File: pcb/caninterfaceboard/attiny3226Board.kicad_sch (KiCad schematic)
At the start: 64 parts, among them J10 NTC2, J12 Flywheel, J13 1Wire, J2 CAN, J3 Attiny UDPI, J4 NTC3, J5 12V In, J6 FuelLevel, J7 Engine, J8 NTC1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

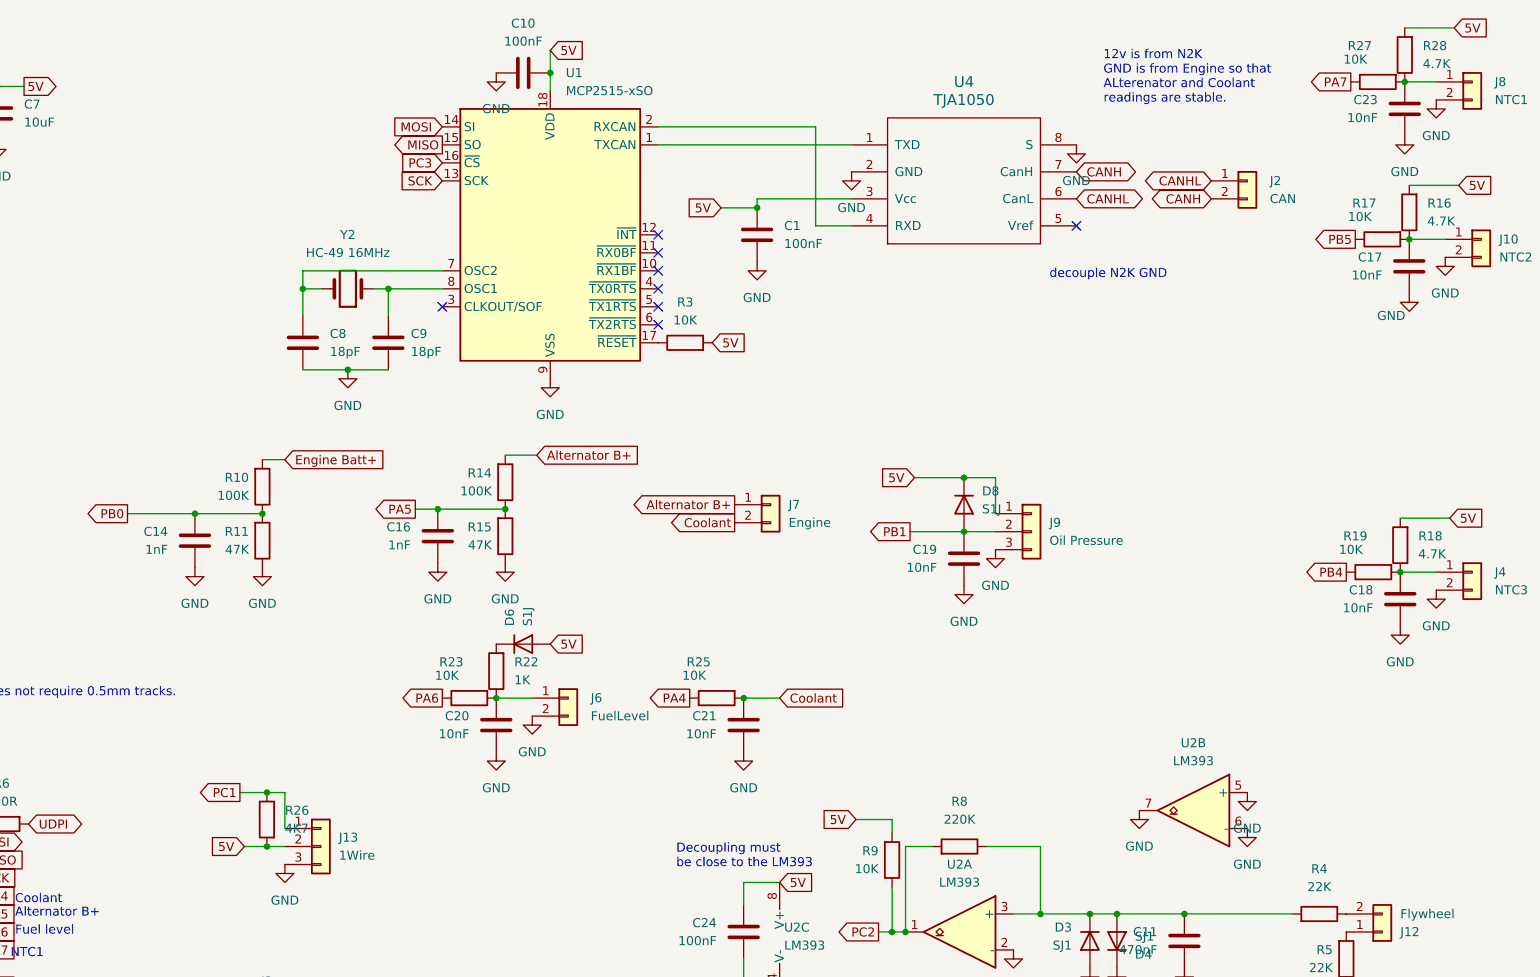
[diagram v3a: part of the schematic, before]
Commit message: Added protection for ovre voltages on measurements
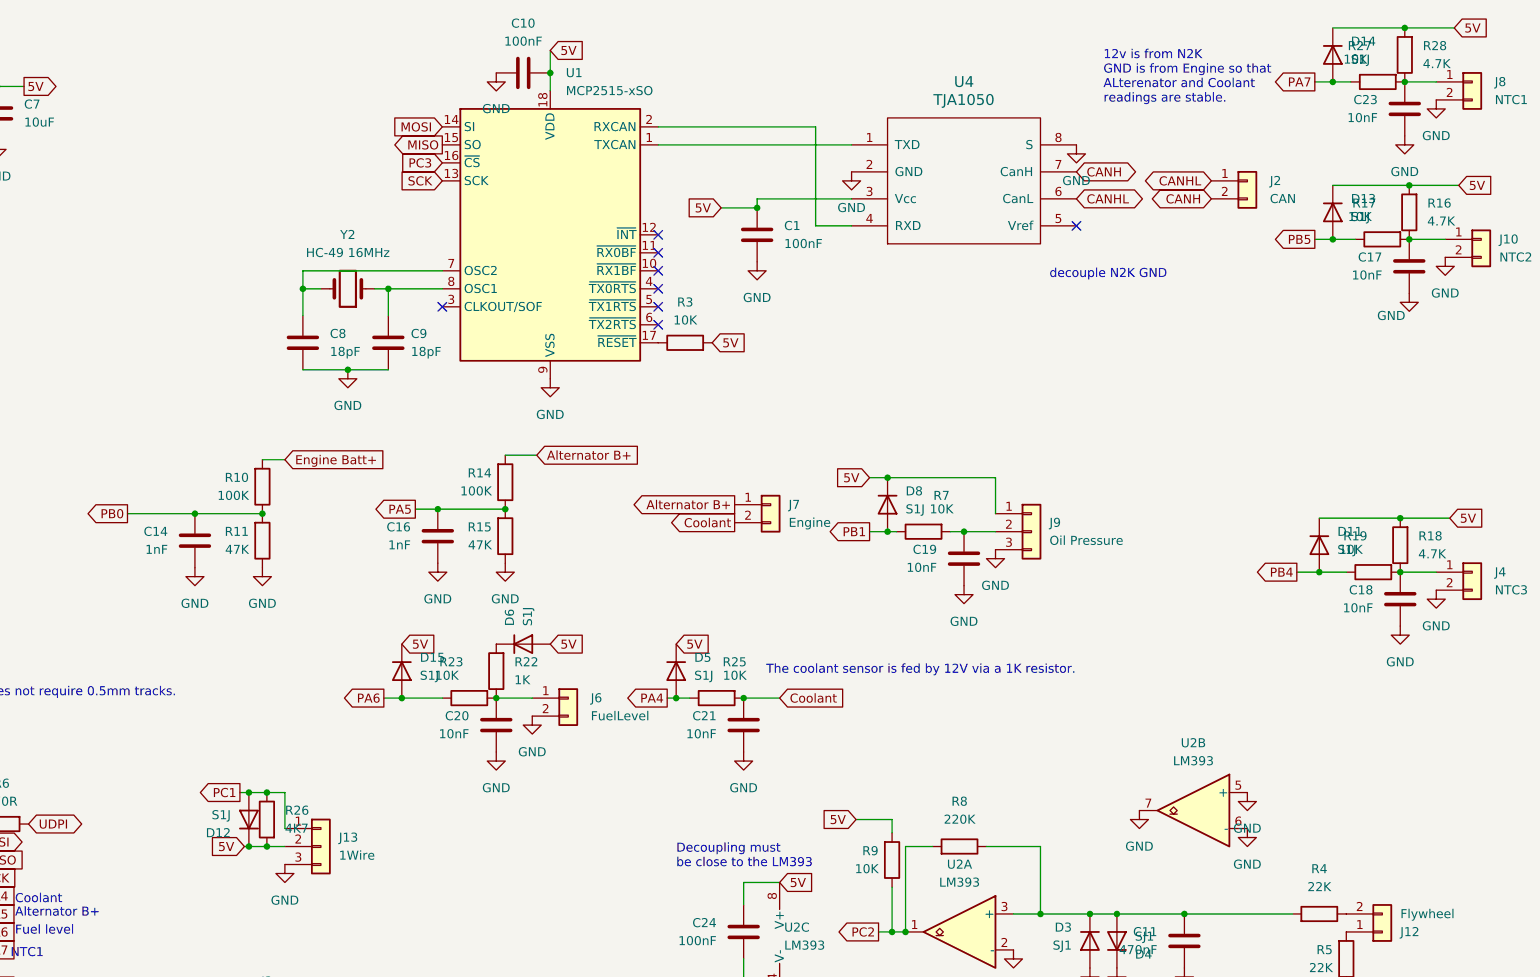
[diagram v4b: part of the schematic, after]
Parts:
- added D11, D12, D13, D14, D15, D5: S1J, Diode_SMD:D_0805_2012Metric_Pad1.15x1.40mm_HandSolder, symbol Device:D
- added R7: 10K, Resistor_SMD:R_0805_2012Metric_Pad1.20x1.40mm_HandSolder, symbol Device:R
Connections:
- net 5V: now also D11.1 (K), D12.1 (K), D13.1 (K), D14.1 (K), D15.1 (K), D5.1 (K)
- net PA4: now also D5.2 (A)
- net PA6: now also D15.2 (A)
- net PA7: now also D14.2 (A)
- net PB1: now also R7.1; no longer C19.2, J9.2 (Pin_2)
- net PB4: now also D11.2 (A)
- net PB5: now also D13.2 (A)
- net PC1: now also D12.2 (A)
- new net: C19.2, J9.2 (Pin_2), R7.2
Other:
- note added: "The coolant sensor is fed by 12V via a 1K resistor."
- moved on the sheet: D8

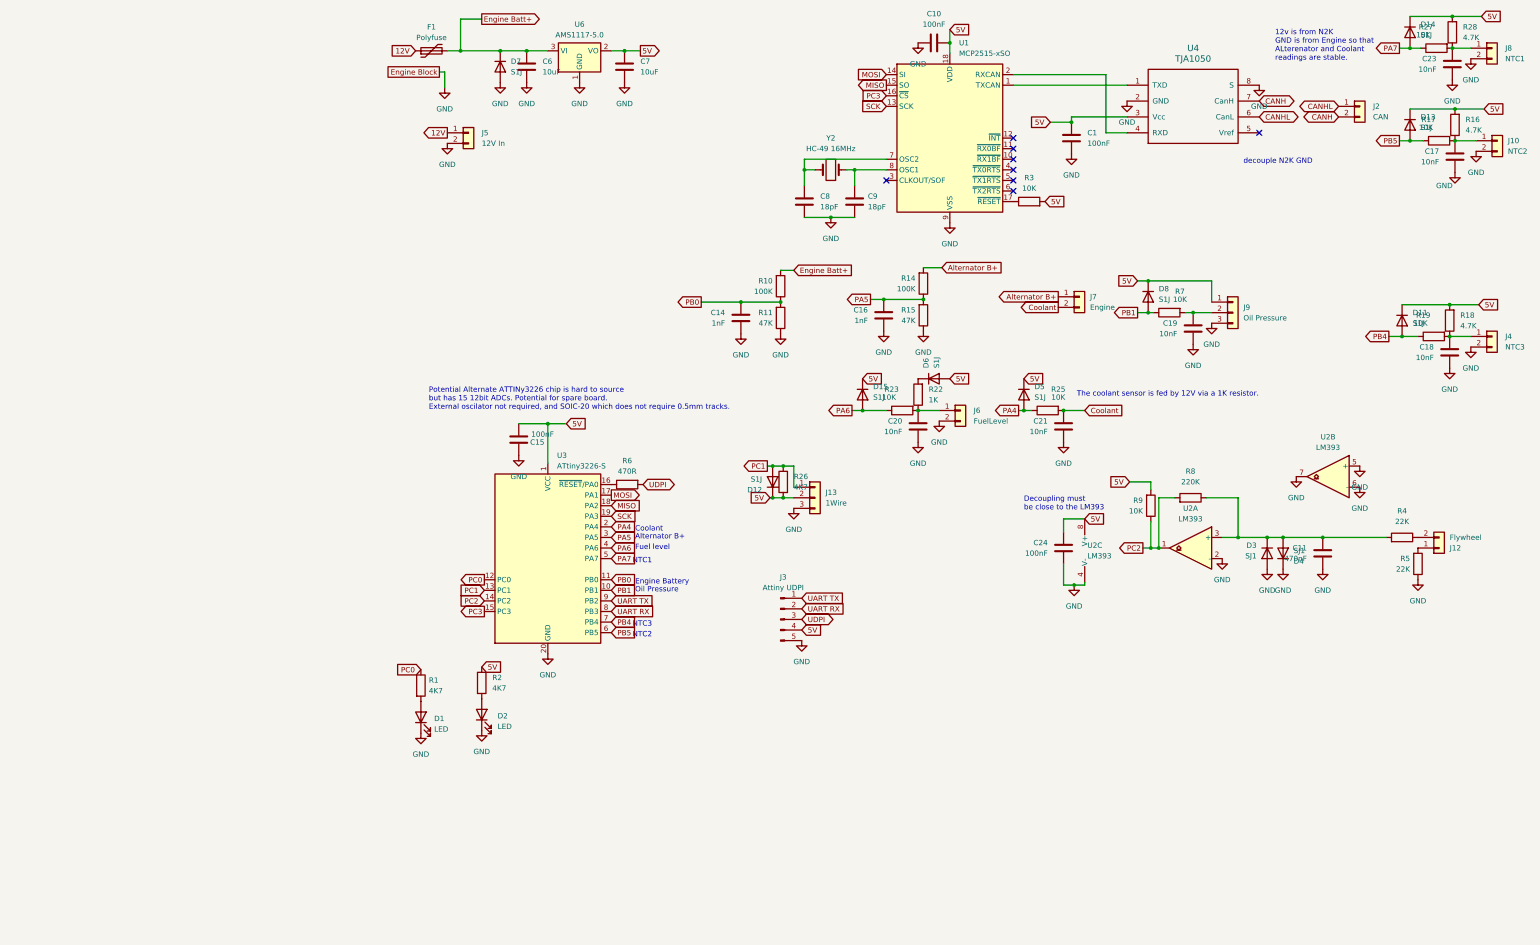
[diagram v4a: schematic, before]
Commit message: Improvd ADC stability
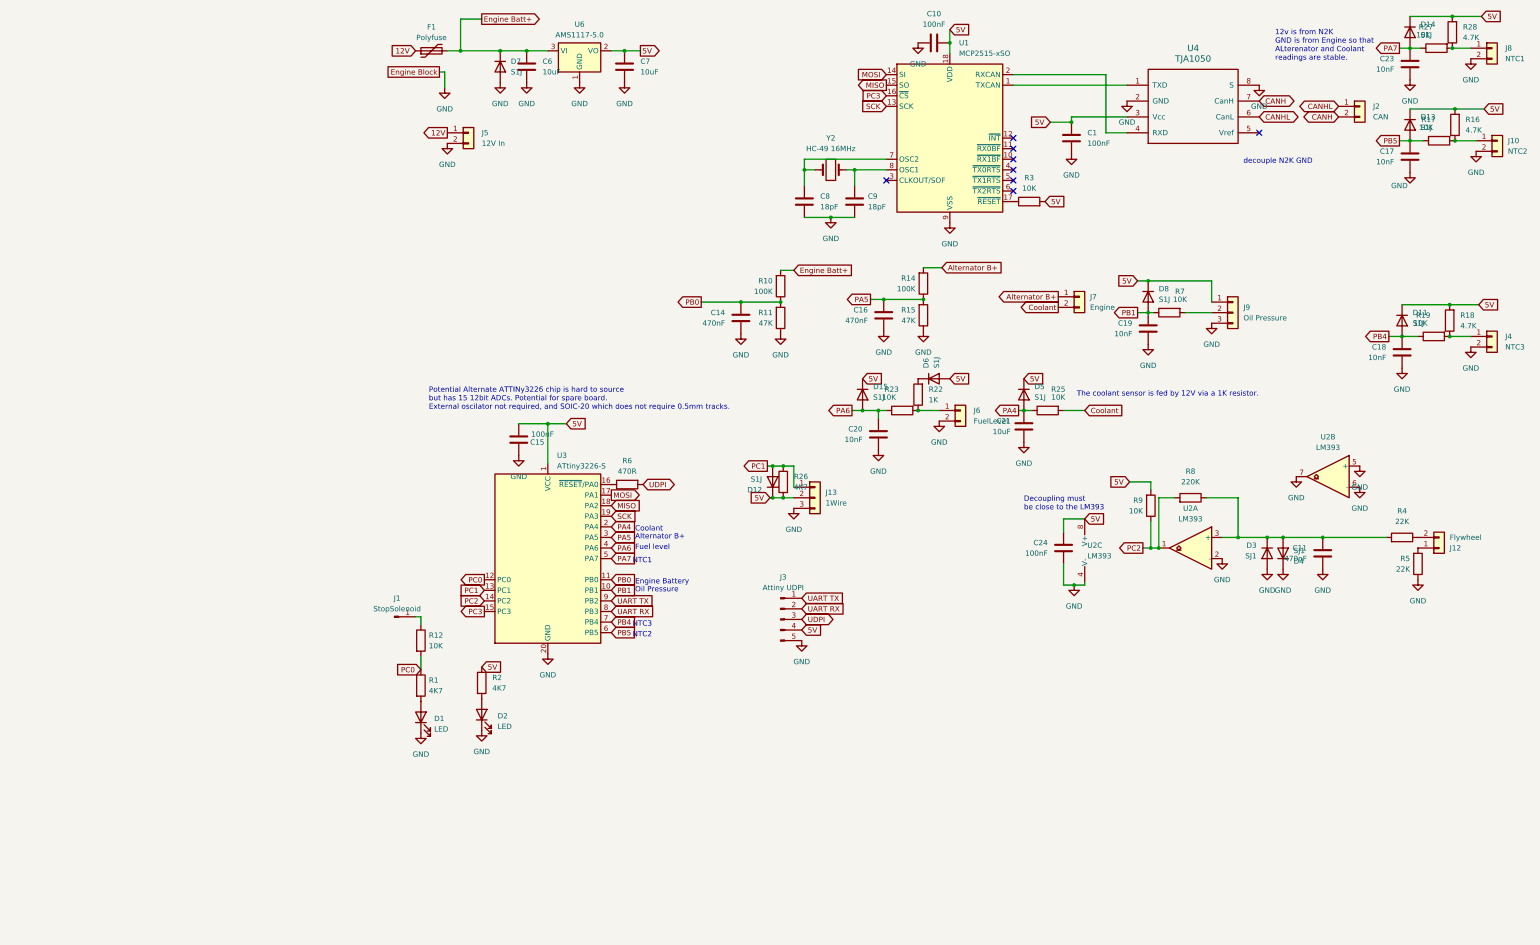
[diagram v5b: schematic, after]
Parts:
- added J1: StopSolenoid, Connector_PinSocket_2.54mm:PinSocket_1x01_P2.54mm_Vertical, symbol Connector:Conn_01x01_Pin
- added R12: 10K, Resistor_SMD:R_0805_2012Metric_Pad1.20x1.40mm_HandSolder, symbol Device:R
- C14, C16: value 1nF -> 470nF
- C21: value 10nF -> 10uF
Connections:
- net Coolant: no longer C21.2
- net PA4: now also C21.2
- net PA6: now also C20.2
- net PA7: now also C23.2
- net PB1: now also C19.2
- net PB4: now also C18.2
- net PB5: now also C17.2
- net PC0: now also R12.2
- net at J8.1 (Pin_1), R27.2, R28.1: no longer C23.2
- net at J6.1 (Pin_1), R22.1, R23.2: no longer C20.2
- net at J10.1 (Pin_1), R16.1, R17.2: no longer C17.2
- net at J4.1 (Pin_1), R18.1, R19.2: no longer C18.2
- net at J9.2 (Pin_2), R7.2: no longer C19.2
- new net: J1.1 (Pin_1), R12.1
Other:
- moved on the sheet: C17, C18, C19, C20, C21, C23

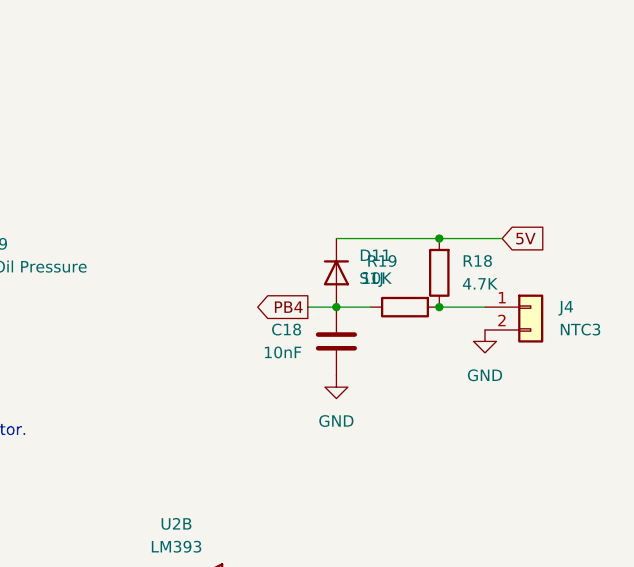
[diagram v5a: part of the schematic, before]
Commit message: Fixed spurious alarms
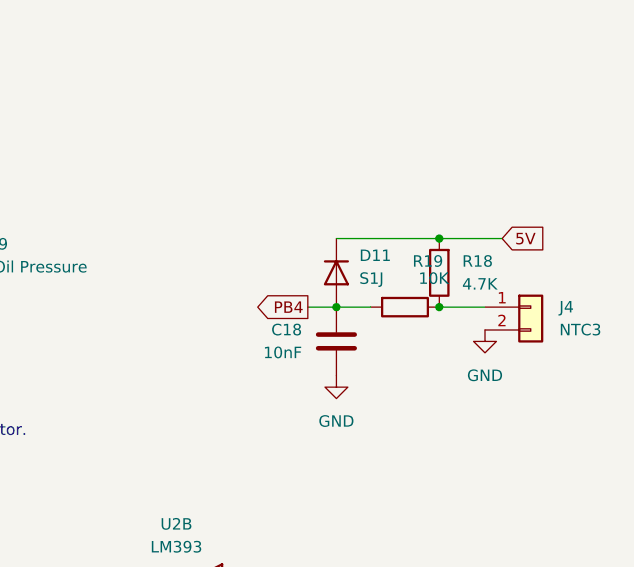
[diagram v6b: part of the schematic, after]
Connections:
- net PB4: now also R19.2; no longer R19.1
- net at J4.1 (Pin_1), R18.1: now also R19.1; no longer R19.2
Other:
- moved on the sheet: R19
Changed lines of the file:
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@@
     )
   )
-  (symbol (lib_id "Device:R") (at 266.7 92.075 90) (mirror x) (unit 1)
+  (symbol (lib_id "Device:R") (at 266.7 92.075 270) (unit 1)
     (in_bom yes) (on_board yes) (dnp no)
-    (property "Reference" "R19" (at 264.16 86.995 90)
+    (property "Reference" "R19" (at 269.24 86.995 90)
       (effects (font (size 1.27 1.27)))
     )
-    (property "Value" "10K" (at 263.525 88.9 90)
+    (property "Value" "10K" (at 269.875 88.9 90)
       (effects (font (size 1.27 1.27)))
     )

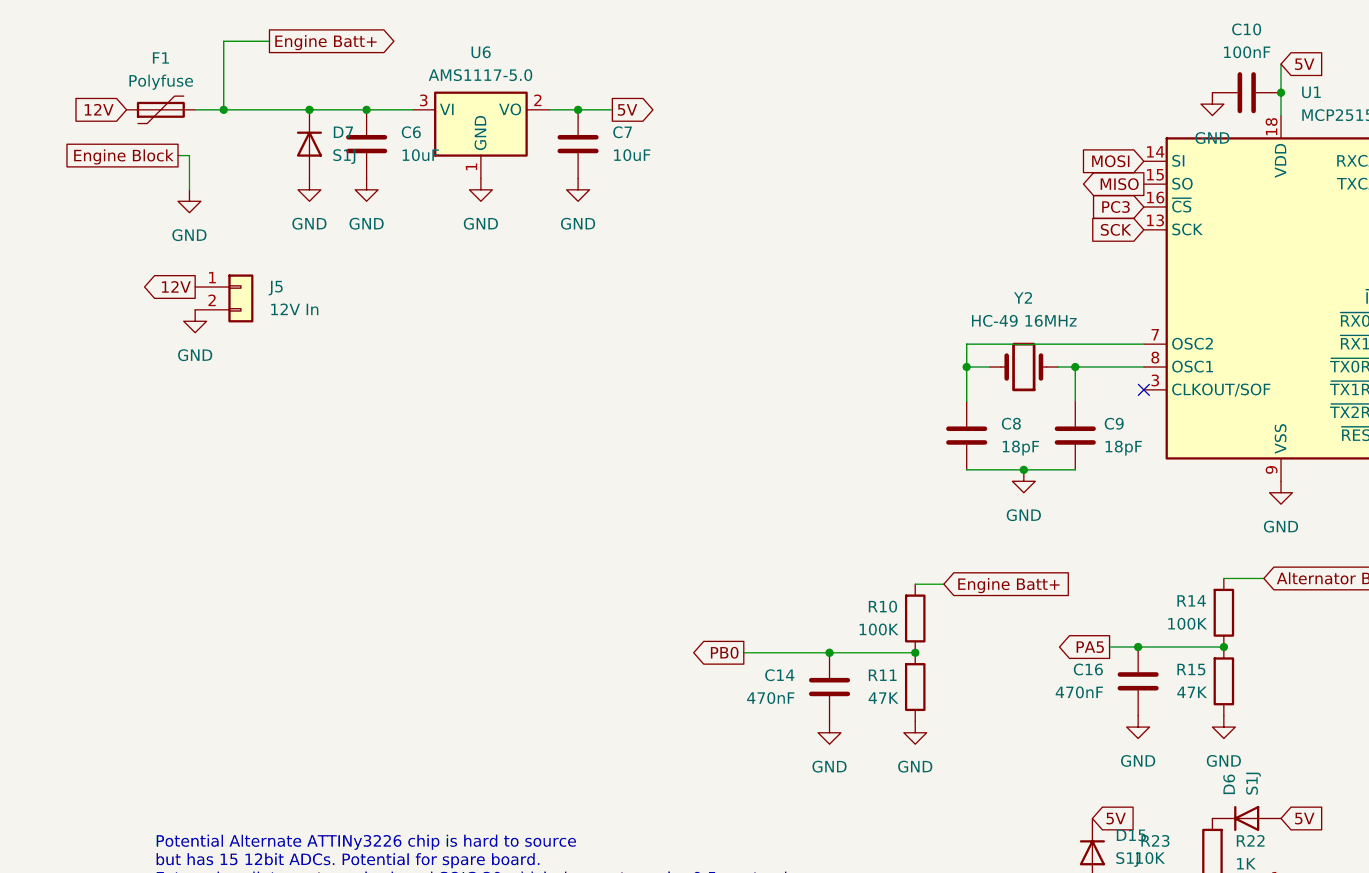
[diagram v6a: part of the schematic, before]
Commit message: Improved voltage sampling
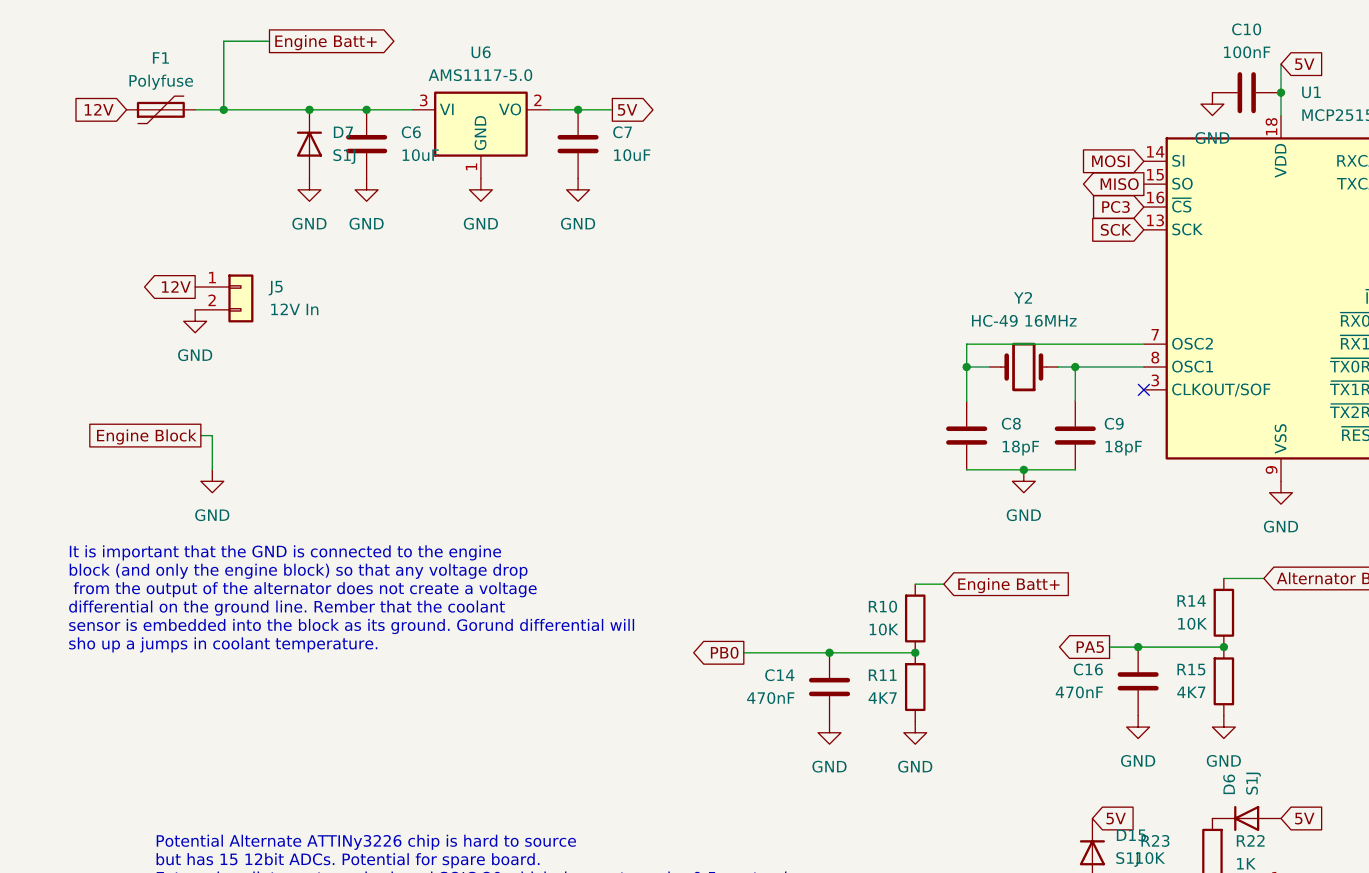
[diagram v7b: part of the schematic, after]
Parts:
- R10, R14: value 100K -> 10K
- R11, R15: value 47K -> 4K7
- Y2: value HC-49 16MHz -> HC-49 16MHz
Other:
- note added: "It is important that the GND is connected to the engine block (and only the engine block) so that any voltage drop from the output of the alternator does not create a voltage differential on the ground line. Rember that the coolant sensor is embedded into the block as its ground. Gorund differential will sho up a jumps in coolant temperature."
